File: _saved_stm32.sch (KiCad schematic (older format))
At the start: 18 parts, among them CON1 BARREL_JACK, P1 CONN_01X11, P2 CONN_01X13, P3 CONN_01X08, P4 CONN_01X14, U1 STM32F103RB, U2 LD1117S33TR

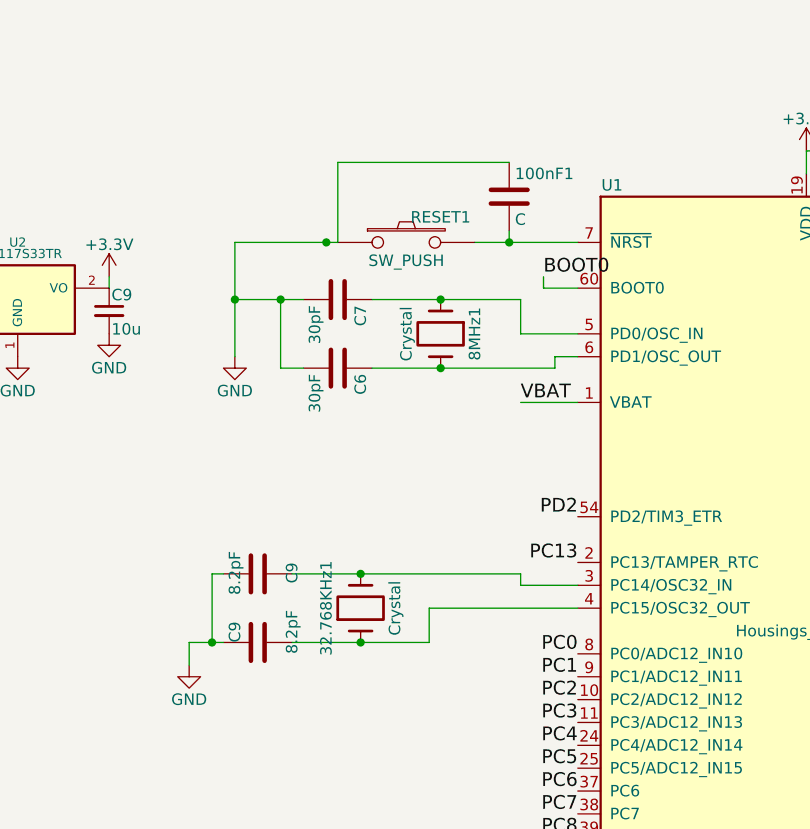
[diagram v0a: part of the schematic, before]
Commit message: ajustes
corrigido a inversão do valor com referencia
diminuido a largura da trilha.
trocado componentes por smd
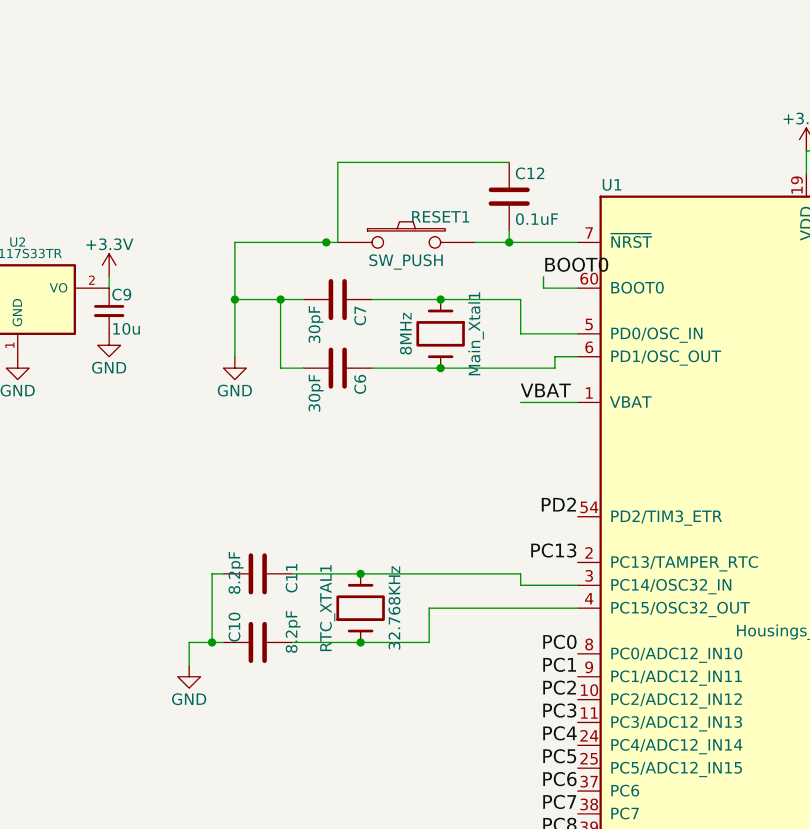
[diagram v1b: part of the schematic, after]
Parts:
- C10, C11: renamed from C9; footprint Capacitors_SMD:C_0603_HandSoldering -> Capacitors_SMD:C_0805_HandSoldering
- C12: renamed from 100nF1; value C -> 0.1uF; footprint Capacitors_SMD:C_0603_HandSoldering -> Capacitors_SMD:C_0805_HandSoldering
- C6, C7, C8, C9: footprint Capacitors_SMD:C_0603_HandSoldering -> Capacitors_SMD:C_0805_HandSoldering
- Main_Xtal1: renamed from 8MHz1; value Crystal -> 8MHz; footprint Crystals:HC-18UV -> Crystals:Crystal_HC49-SD_SMD
- RTC_XTAL1: renamed from 32.768KHz1; value Crystal -> 32.768KHz
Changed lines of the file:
@@
 $EndComp
 $Comp
-L Crystal 32.768KHz1
+L Crystal RTC_XTAL1
 U 1 1 5717BE05
 P 3850 3950
-F 0 "32.768KHz1" H 3850 4100 50  0000 C CNN
-F 1 "Crystal" H 3850 3800 50  0000 C CNN
+F 0 "RTC_XTAL1" H 3850 4100 50  0000 C CNN
+F 1 "32.768KHz" H 3850 3800 50  0000 C CNN
 F 2 "Crystals:Crystal_Round_Vertical_3mm" H 3850 3950 50  0001 C CNN
 F 3 "" H 3850 3950 50  0000 C CNN
@@
 $EndComp
 $Comp
-L C C9
+L C C11
 U 1 1 5717BF02
 P 3400 3800
-F 0 "C9" H 3350 3950 50  0000 L CNN
+F 0 "C11" H 3350 3950 50  0000 L CNN
 F 1 "8.2pF" H 3300 3700 50  0000 L CNN
-F 2 "Capacitors_SMD:C_0603_HandSoldering" H 3438 3650 50  0001 C CNN
+F 2 "Capacitors_SMD:C_0805_HandSoldering" H 3438 3650 50  0001 C CNN
 F 3 "" H 3400 3800 50  0000 C CNN
 	1    3400 3800
@@
 $EndComp
 $Comp
-L C C9
+L C C10
 U 1 1 5717BFEF
 P 3400 4100
-F 0 "C9" H 3400 4200 50  0000 L CNN
+F 0 "C10" H 3400 4200 50  0000 L CNN
 F 1 "8.2pF" H 3350 3950 50  0000 L CNN
-F 2 "Capacitors_SMD:C_0603_HandSoldering" H 3438 3950 50  0001 C CNN
+F 2 "Capacitors_SMD:C_0805_HandSoldering" H 3438 3950 50  0001 C CNN
 F 3 "" H 3400 4100 50  0000 C CNN
 	1    3400 4100
@@
 $EndComp
 $Comp
-L C 100nF1
+L C C12
 U 1 1 57182019
 P 4500 2150
-F 0 "100nF1" H 4525 2250 50  0000 L CNN
-F 1 "C" H 4525 2050 50  0000 L CNN
-F 2 "Capacitors_SMD:C_0603_HandSoldering" H 4538 2000 50  0001 C CNN
+F 0 "C12" H 4525 2250 50  0000 L CNN
+F 1 "0.1uF" H 4525 2050 50  0000 L CNN
+F 2 "Capacitors_SMD:C_0805_HandSoldering" H 4538 2000 50  0001 C CNN
 F 3 "" H 4500 2150 50  0000 C CNN
 	1    4500 2150
@@
 $EndComp
 $Comp
-L Crystal 8MHz1
+L Crystal Main_Xtal1
 U 1 1 57184B59
 P 4200 2750
-F 0 "8MHz1" H 4200 2900 50  0000 C CNN
-F 1 "Crystal" H 4200 2600 50  0000 C CNN
-F 2 "Crystals:HC-18UV" H 4200 2750 50  0001 C CNN
+F 0 "Main_Xtal1" H 4200 2900 50  0000 C CNN
+F 1 "8MHz" H 4200 2600 50  0000 C CNN
+F 2 "Crystals:Crystal_HC49-SD_SMD" H 4200 2750 50  0001 C CNN
 F 3 "" H 4200 2750 50  0000 C CNN
 	1    4200 2750
@@
 F 0 "C7" H 3775 2700 50  0000 L CNN
 F 1 "30pF" H 3775 2500 50  0000 L CNN
-F 2 "Capacitors_SMD:C_0603_HandSoldering" H 3788 2450 50  0001 C CNN
+F 2 "Capacitors_SMD:C_0805_HandSoldering" H 3788 2450 50  0001 C CNN
 F 3 "" H 3750 2600 50  0000 C CNN
 	1    3750 2600
@@
 F 0 "C6" H 3775 3000 50  0000 L CNN
 F 1 "30pF" H 3775 2800 50  0000 L CNN
-F 2 "Capacitors_SMD:C_0603_HandSoldering" H 3788 2750 50  0001 C CNN
+F 2 "Capacitors_SMD:C_0805_HandSoldering" H 3788 2750 50  0001 C CNN
 F 3 "" H 3750 2900 50  0000 C CNN
 	1    3750 2900
@@
 F 0 "C8" H 1960 2720 50  0000 L CNN
 F 1 "10u" H 1960 2570 50  0000 L CNN
-F 2 "Capacitors_SMD:C_0603_HandSoldering" H 1950 2650 60  0001 C CNN
+F 2 "Capacitors_SMD:C_0805_HandSoldering" H 1950 2650 60  0001 C CNN
 F 3 "" H 1950 2650 60  0000 C CNN
 	1    1950 2650
@@
 F 0 "C9" H 2760 2720 50  0000 L CNN
 F 1 "10u" H 2760 2570 50  0000 L CNN
-F 2 "Capacitors_SMD:C_0603_HandSoldering" H 2750 2650 60  0001 C CNN
+F 2 "Capacitors_SMD:C_0805_HandSoldering" H 2750 2650 60  0001 C CNN
 F 3 "" H 2750 2650 60  0000 C CNN
 	1    2750 2650
